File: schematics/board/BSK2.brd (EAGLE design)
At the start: 82 x 100 mm, 26 parts

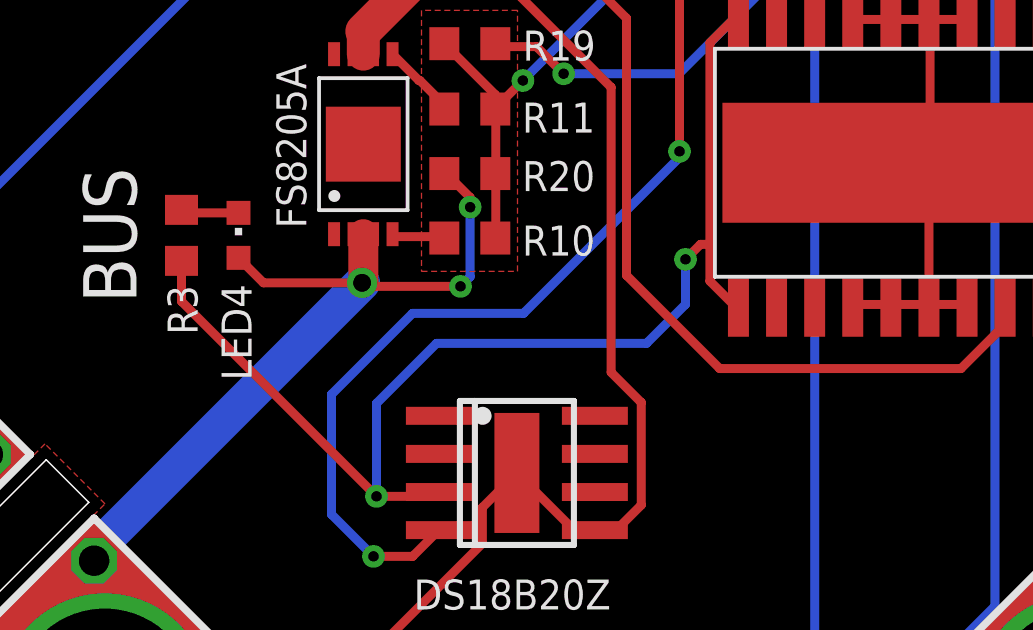
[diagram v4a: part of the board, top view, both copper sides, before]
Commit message: Исправлены RADIO и диоды
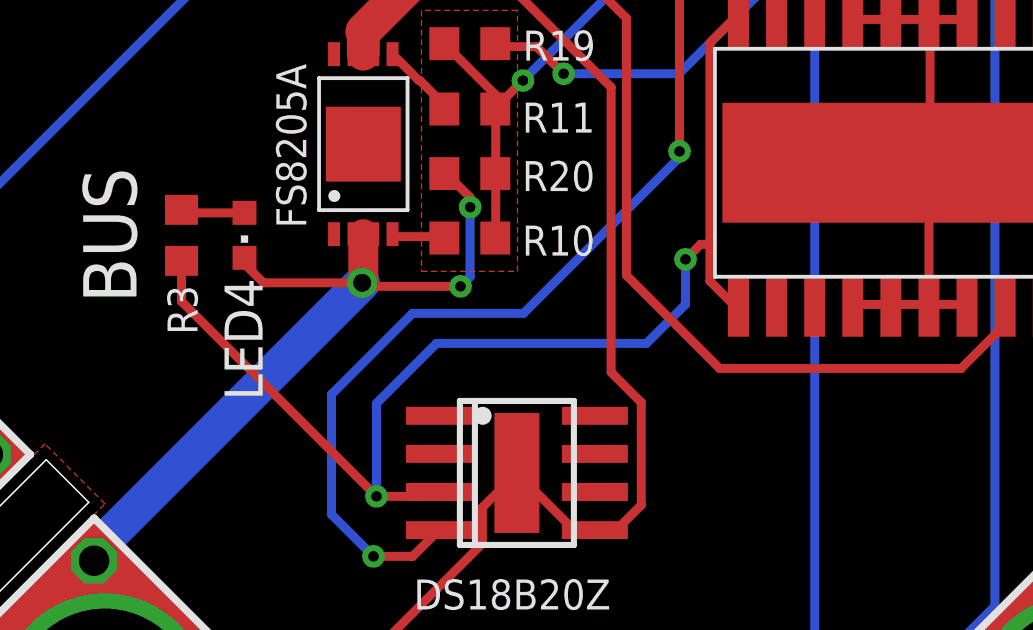
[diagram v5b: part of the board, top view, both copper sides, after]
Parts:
- moved LED4 0.20 mm to (29.4, 81.7), turned to 180 degrees
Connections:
- net BUS-: now also LED4.C; no longer LED4.A
- net N$25: now also LED4.A; no longer LED4.C
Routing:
- net GND: track 111.7 -> 111.0 mm
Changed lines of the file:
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@@
 <attribute name="VALUE" x="14.405" y="64.63" size="1.27" layer="27" rot="R90"/>
-</element>
-<element name="LED4" library="led" library_urn="urn:adsk.eagle:library:259" package="CHIPLED_0603" package3d_urn="urn:adsk.eagle:package:15822/2" value="" x="29.2" y="81.7" smashed="yes">
-<attribute name="NAME" x="28.635" y="80.07" size="1" layer="25" rot="R270"/>
-<attribute name="POPULARITY" value="28" x="9.6" y="78" size="1.778" layer="27" display="off"/>
-<attribute name="VALUE" x="31.105" y="80.43" size="1.27" layer="27" rot="R90"/>
 </element>
 <element name="R3" library="resistor" library_urn="urn:adsk.eagle:library:348" package="R0603" package3d_urn="urn:adsk.eagle:package:23555/3" value="2k" x="27.3" y="81.7" smashed="yes" rot="R90">
 <attribute name="NAME" x="26.835" y="80.035" size="1" layer="25" rot="R270"/>
 <attribute name="VALUE" x="29.205" y="81.065" size="1.27" layer="27" rot="R90"/>
+</element>
+<element name="LED4" library="led" library_urn="urn:adsk.eagle:library:259" package="CHIPLED_0603" package3d_urn="urn:adsk.eagle:package:15822/2" value="" x="29.4" y="81.7" smashed="yes" rot="R180">
+<attribute name="NAME" x="28.735" y="80.27" size="1.27" layer="25" rot="R270"/>
+<attribute name="POPULARITY" value="28" x="34.4" y="76.2" size="1.778" layer="27" rot="R180" display="off"/>
+<attribute name="VALUE" x="27.495" y="82.97" size="1.27" layer="27" rot="R270"/>
 </element>
 </elements>
@@
 <wire x1="53.3832" y1="79.3962" x2="53.485" y2="79.32" width="0.3" layer="1"/>
 <wire x1="52.2522" y1="79.3962" x2="52.215" y2="79.32" width="0.3" layer="1"/>
-<wire x1="49.5378" y1="79.17" x2="49.5378" y2="78.4914" width="0.3" layer="1"/>
 <wire x1="49.5378" y1="79.17" x2="49.675" y2="79.32" width="0.3" layer="1"/>
 <wire x1="49.5378" y1="90.58" x2="49.5378" y2="89.1228" width="0.3" layer="1"/>
@@
 <wire x1="24.4296" y1="66.5028" x2="24.74" y2="66.26" width="0.3" layer="1"/>
 <via x="33.3204" y="80.1176" extent="1-16" drill="0.6"/>
-<contactref element="LED4" pad="A"/>
 <wire x1="36.92115" y1="82.96485" x2="36.92115" y2="82.63885" width="0.3" layer="1"/>
 <via x="36.92115" y="82.63885" extent="1-16" drill="0.35"/>
@@
 <wire x1="36.192" y1="83.694" x2="36.92115" y2="82.96485" width="0.3" layer="1"/>
 <wire x1="33.3204" y1="80.1176" x2="30.0324" y2="80.1176" width="0.3" layer="1"/>
-<wire x1="30.0324" y1="80.1176" x2="29.2" y2="80.95" width="0.3" layer="1"/>
 <wire x1="33.3204" y1="80.1176" x2="33.36" y2="80.1572" width="1" layer="1"/>
 <wire x1="33.36" y1="80.1572" x2="33.36" y2="81.74" width="1" layer="1"/>
+<contactref element="LED4" pad="C"/>
+<wire x1="30.0324" y1="80.1176" x2="29.4" y2="80.75" width="0.3" layer="1"/>
+<wire x1="29.4" y1="80.75" x2="29.4" y2="80.95" width="0.3" layer="1"/>
 </signal>
 <signal name="N$8">
@@
 </signal>
 <signal name="N$25">
+<contactref element="LED4" pad="A"/>
 <contactref element="R3" pad="2"/>
-<contactref element="LED4" pad="C"/>
-<wire x1="29.2" y1="82.45" x2="27.4" y2="82.45" width="0.3" layer="1"/>
+<wire x1="29.4" y1="82.45" x2="27.4" y2="82.45" width="0.3" layer="1"/>
 <wire x1="27.4" y1="82.45" x2="27.3" y2="82.55" width="0.3" layer="1"/>
 </signal>

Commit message: Резисторы у FS8205A 100Ом
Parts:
- R10, R11: value 10k -> 100R
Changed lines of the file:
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@@
 </autorouter>
 <elements>
-<element name="R10" library="resistor" library_urn="urn:adsk.eagle:library:348" package="R0603" package3d_urn="urn:adsk.eagle:package:23555/3" value="10k" x="36.91" y="81.61" smashed="yes" rot="R180">
+<element name="R10" library="resistor" library_urn="urn:adsk.eagle:library:348" package="R0603" package3d_urn="urn:adsk.eagle:package:23555/3" value="100R" x="36.91" y="81.61" smashed="yes" rot="R180">
 <attribute name="NAME" x="38.655" y="81.025" size="1" layer="25"/>
 <attribute name="VALUE" x="37.545" y="83.515" size="1.27" layer="27" rot="R180"/>
 </element>
-<element name="R11" library="resistor" library_urn="urn:adsk.eagle:library:348" package="R0603" package3d_urn="urn:adsk.eagle:package:23555/3" value="10k" x="36.91" y="85.91" smashed="yes" rot="R180">
+<element name="R11" library="resistor" library_urn="urn:adsk.eagle:library:348" package="R0603" package3d_urn="urn:adsk.eagle:package:23555/3" value="100R" x="36.91" y="85.91" smashed="yes" rot="R180">
 <attribute name="NAME" x="38.655" y="85.125" size="1" layer="25"/>
 <attribute name="VALUE" x="37.545" y="87.815" size="1.27" layer="27" rot="R180"/>

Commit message: Добавлены новые диоды
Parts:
- added LAP4: LAP4-BOTTOM, led:P47F-BOTTOM
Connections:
- net BUS-: now also LAP4.C
- net N$25: now also LAP4.A
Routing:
- net N$25: track 2.14 -> 77.5 mm, vias 0 -> 2
- net BUS-: track 45.3 -> 86.2 mm, vias 3 -> 4
